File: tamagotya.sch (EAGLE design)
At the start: 34 parts, among them U100 ESP32-D2WD, U200 UT-0206-P05FOLDED, U300 4MB Flash, Y100 40Mhz 3.2X2.5

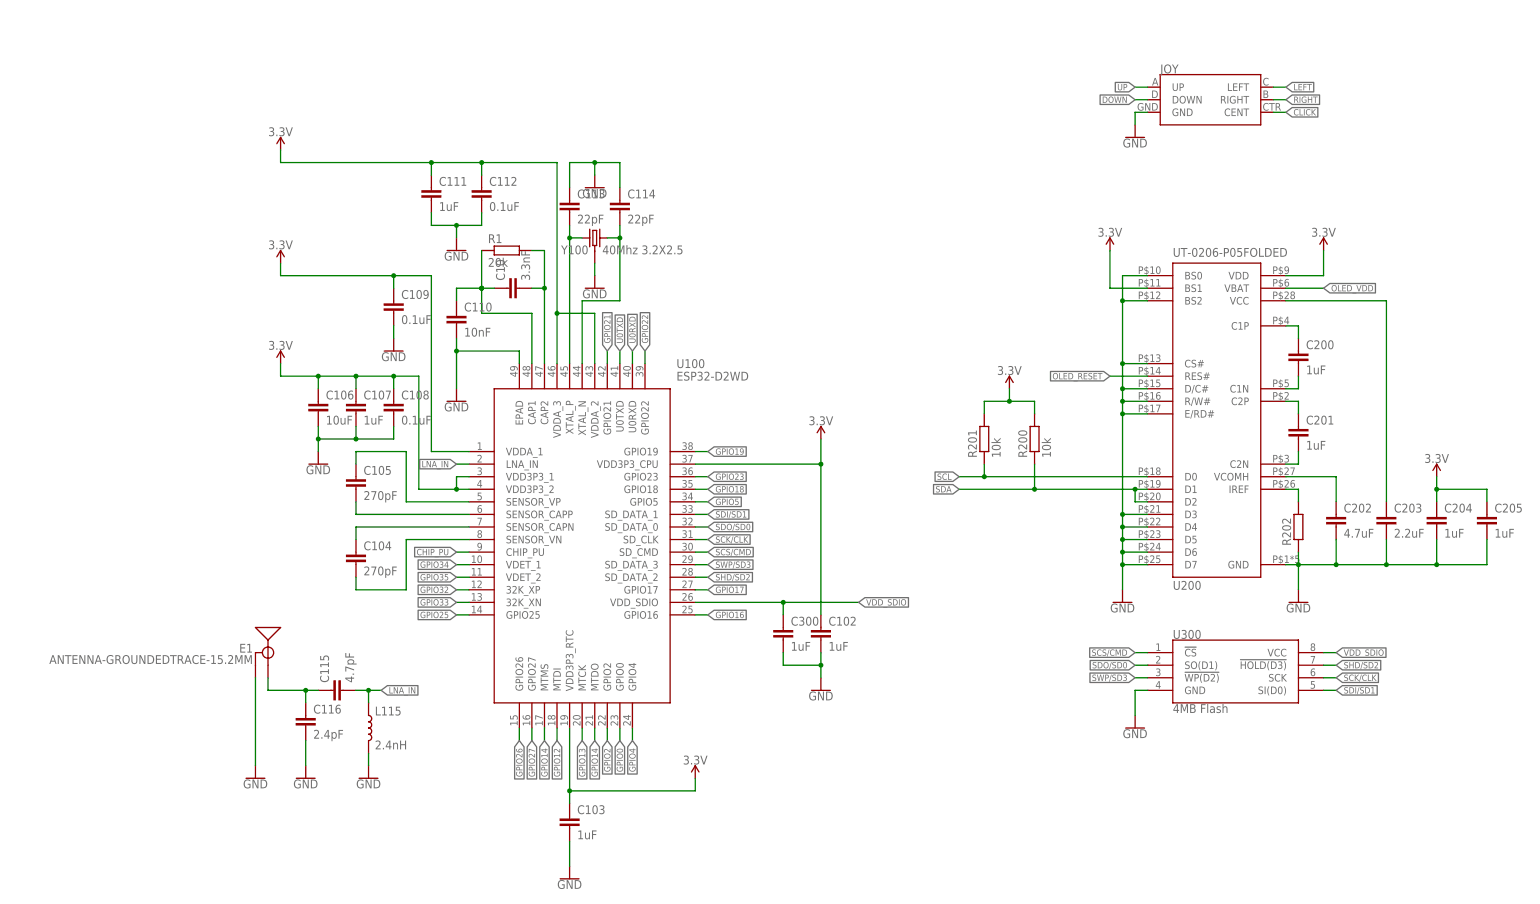
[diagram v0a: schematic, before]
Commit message: Laid out, need to add charge/boost circuit and its basically done. Could do with a UART too.
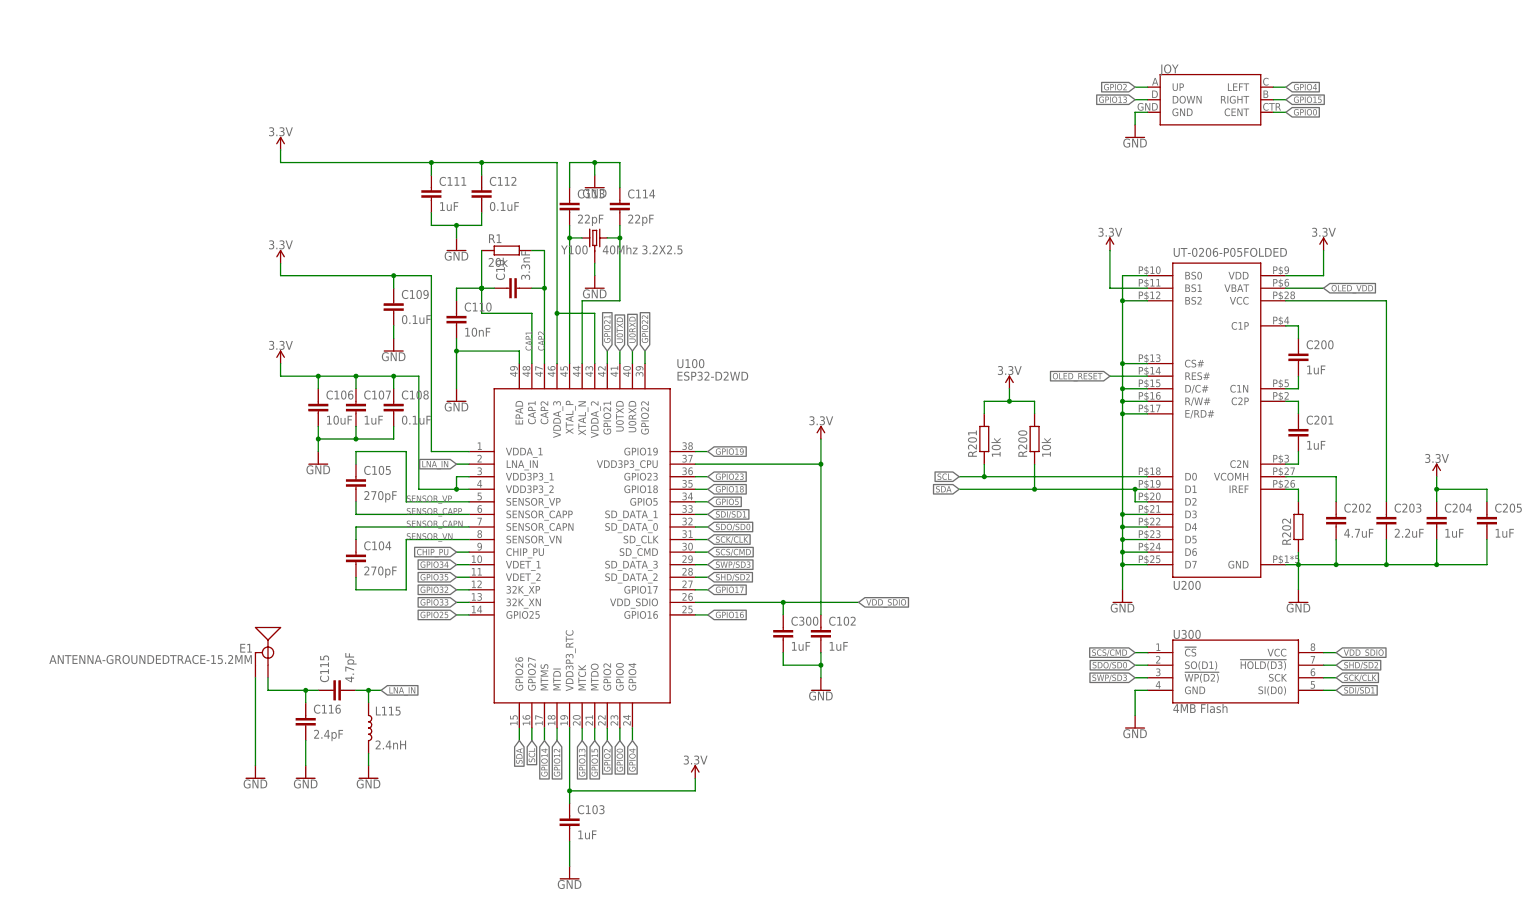
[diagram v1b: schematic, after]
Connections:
- net N$1 renamed SENSOR_VN
- net N$2 renamed SENSOR_CAPN
- net N$3 renamed SENSOR_VP
- net N$4 renamed SENSOR_CAPP
- net N$8 renamed CAP1
- net N$9 renamed CAP2
- removed net CLICK: JOY.CENT
- removed net DOWN: JOY.DOWN
- removed net GPIO26: U100.GPIO26
- removed net GPIO27: U100.GPIO27
- removed net LEFT: JOY.LEFT
- removed net RIGHT: JOY.RIGHT
- removed net UP: JOY.UP
- new net GPIO15: JOY.RIGHT, U100.MTDO
- net GPIO0: now also JOY.CENT
- net GPIO13: now also JOY.DOWN
- net GPIO14: no longer U100.MTDO
- net GPIO2: now also JOY.UP
- net GPIO4: now also JOY.LEFT
- net SCL: now also U100.GPIO27
- net SDA: now also U100.GPIO26
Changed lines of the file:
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@@
 <?xml version="1.0" encoding="utf-8"?>
 <!DOCTYPE eagle SYSTEM "eagle.dtd">
-<eagle version="9.2.2">
+<eagle version="9.3.0">
 <drawing>
 <settings>
-<setting alwaysvectorfont="yes"/>
+<setting alwaysvectorfont="no"/>
 <setting verticaltext="up"/>
 </settings>
@@
 </segment>
 </net>
-<net name="GPIO26" class="0">
-<segment>
-<pinref part="U100" gate="G$1" pin="GPIO26"/>
-<wire x1="58.42" y1="33.02" x2="58.42" y2="30.48" width="0.1524" layer="91"/>
-<label x="58.42" y="30.48" size="1.27" layer="95" rot="R270" xref="yes"/>
-</segment>
-</net>
-<net name="GPIO27" class="0">
-<segment>
-<pinref part="U100" gate="G$1" pin="GPIO27"/>
-<wire x1="60.96" y1="33.02" x2="60.96" y2="30.48" width="0.1524" layer="91"/>
-<label x="60.96" y="30.48" size="1.27" layer="95" rot="R270" xref="yes"/>
-</segment>
-</net>
 <net name="GPIO14" class="0">
 <segment>
@@
 <label x="63.5" y="30.48" size="1.27" layer="95" rot="R270" xref="yes"/>
 </segment>
-<segment>
-<pinref part="U100" gate="G$1" pin="MTDO"/>
-<wire x1="73.66" y1="33.02" x2="73.66" y2="30.48" width="0.1524" layer="91"/>
-<label x="73.66" y="30.48" size="1.27" layer="95" rot="R270" xref="yes"/>
-</segment>
 </net>
 <net name="GPIO12" class="0">
@@
 <label x="71.12" y="30.48" size="1.27" layer="95" rot="R270" xref="yes"/>
 </segment>
+<segment>
+<pinref part="JOY" gate="G$1" pin="DOWN"/>
+<wire x1="185.42" y1="160.02" x2="182.88" y2="160.02" width="0.1524" layer="91"/>
+<label x="182.88" y="160.02" size="1.27" layer="95" rot="R180" xref="yes"/>
+</segment>
 </net>
 <net name="GPIO2" class="0">
@@
 <label x="76.2" y="30.48" size="1.27" layer="95" rot="R270" xref="yes"/>
 </segment>
+<segment>
+<pinref part="JOY" gate="G$1" pin="UP"/>
+<wire x1="185.42" y1="162.56" x2="182.88" y2="162.56" width="0.1524" layer="91"/>
+<label x="182.88" y="162.56" size="1.27" layer="95" rot="R180" xref="yes"/>
+</segment>
 </net>
 <net name="GPIO0" class="0">
@@
 <label x="78.74" y="30.48" size="1.27" layer="95" rot="R270" xref="yes"/>
 </segment>
+<segment>
+<pinref part="JOY" gate="G$1" pin="CENT"/>
+<wire x1="210.82" y1="157.48" x2="213.36" y2="157.48" width="0.1524" layer="91"/>
+<label x="213.36" y="157.48" size="1.27" layer="95" xref="yes"/>
+</segment>
 </net>
 <net name="GPIO4" class="0">
@@
 <label x="81.28" y="30.48" size="1.27" layer="95" rot="R270" xref="yes"/>
 </segment>
+<segment>
+<pinref part="JOY" gate="G$1" pin="LEFT"/>
+<wire x1="210.82" y1="162.56" x2="213.36" y2="162.56" width="0.1524" layer="91"/>
+<label x="213.36" y="162.56" size="1.27" layer="95" xref="yes"/>
+</segment>
 </net>
 <net name="GPIO25" class="0">
@@
 </segment>
 </net>
-<net name="N$1" class="0">
+<net name="SENSOR_VN" class="0">
 <segment>
 <pinref part="U100" gate="G$1" pin="SENSOR_VN"/>
@@
 <pinref part="C104" gate="G$1" pin="2"/>
 <wire x1="25.4" y1="60.96" x2="25.4" y2="63.5" width="0.1524" layer="91"/>
-</segment>
-</net>
-<net name="N$2" class="0">
+<label x="35.56" y="71.12" size="1.27" layer="95"/>
+</segment>
+</net>
+<net name="SENSOR_CAPN" class="0">
 <segment>
 <pinref part="U100" gate="G$1" pin="SENSOR_CAPN"/>
@@
 <pinref part="C104" gate="G$1" pin="1"/>
 <wire x1="25.4" y1="71.12" x2="25.4" y2="73.66" width="0.1524" layer="91"/>
-</segment>
-</net>
-<net name="N$4" class="0">
+<label x="35.56" y="73.66" size="1.27" layer="95"/>
+</segment>
+</net>
+<net name="SENSOR_CAPP" class="0">
 <segment>
 <pinref part="U100" gate="G$1" pin="SENSOR_CAPP"/>
@@
 <pinref part="C105" gate="G$1" pin="2"/>
 <wire x1="25.4" y1="76.2" x2="25.4" y2="78.74" width="0.1524" layer="91"/>
-</segment>
-</net>
-<net name="N$3" class="0">
+<label x="35.56" y="76.2" size="1.27" layer="95"/>
+</segment>
+</net>
+<net name="SENSOR_VP" class="0">
 <segment>
 <pinref part="C105" gate="G$1" pin="1"/>
@@
 <pinref part="U100" gate="G$1" pin="SENSOR_VP"/>
 <wire x1="35.56" y1="78.74" x2="48.26" y2="78.74" width="0.1524" layer="91"/>
-</segment>
-</net>
-<net name="N$8" class="0">
+<label x="35.56" y="78.74" size="1.27" layer="95"/>
+</segment>
+</net>
+<net name="CAP1" class="0">
 <segment>
 <pinref part="R1" gate="G$1" pin="1"/>
@@
 <wire x1="45.72" y1="121.92" x2="50.8" y2="121.92" width="0.1524" layer="91"/>
 <junction x="50.8" y="121.92"/>
-</segment>
-</net>
-<net name="N$9" class="0">
+<label x="60.96" y="109.22" size="1.27" layer="95" rot="R90"/>
+</segment>
+</net>
+<net name="CAP2" class="0">
 <segment>
 <pinref part="R1" gate="G$1" pin="2"/>
@@
 <wire x1="63.5" y1="121.92" x2="63.5" y2="106.68" width="0.1524" layer="91"/>
 <junction x="63.5" y="121.92"/>
+<label x="63.5" y="109.22" size="1.27" layer="95" rot="R90"/>
 </segment>
 </net>
@@
 <wire x1="152.4" y1="86.36" x2="152.4" y2="83.82" width="0.1524" layer="91"/>
 <junction x="152.4" y="83.82"/>
+</segment>
+<segment>
+<pinref part="U100" gate="G$1" pin="GPIO27"/>
+<wire x1="60.96" y1="33.02" x2="60.96" y2="30.48" width="0.1524" layer="91"/>
+<label x="60.96" y="30.48" size="1.27" layer="95" rot="R270" xref="yes"/>
 </segment>
 </net>
@@
 <junction x="162.56" y="81.28"/>
 </segment>
+<segment>
+<pinref part="U100" gate="G$1" pin="GPIO26"/>
+<wire x1="58.42" y1="33.02" x2="58.42" y2="30.48" width="0.1524" layer="91"/>
+<label x="58.42" y="30.48" size="1.27" layer="95" rot="R270" xref="yes"/>
+</segment>
 </net>
 <net name="N$10" class="0">
@@
 </segment>
 </net>
-<net name="DOWN" class="0">
-<segment>
-<pinref part="JOY" gate="G$1" pin="DOWN"/>
-<wire x1="185.42" y1="160.02" x2="182.88" y2="160.02" width="0.1524" layer="91"/>
-<label x="182.88" y="160.02" size="1.27" layer="95" rot="R180" xref="yes"/>
-</segment>
-</net>
-<net name="UP" class="0">
-<segment>
-<pinref part="JOY" gate="G$1" pin="UP"/>
-<wire x1="185.42" y1="162.56" x2="182.88" y2="162.56" width="0.1524" layer="91"/>
-<label x="182.88" y="162.56" size="1.27" layer="95" rot="R180" xref="yes"/>
-</segment>
-</net>
-<net name="LEFT" class="0">
-<segment>
-<pinref part="JOY" gate="G$1" pin="LEFT"/>
-<wire x1="210.82" y1="162.56" x2="213.36" y2="162.56" width="0.1524" layer="91"/>
-<label x="213.36" y="162.56" size="1.27" layer="95" xref="yes"/>
-</segment>
-</net>
-<net name="RIGHT" class="0">
+<net name="GPIO15" class="0">
+<segment>
+<pinref part="U100" gate="G$1" pin="MTDO"/>
+<wire x1="73.66" y1="33.02" x2="73.66" y2="30.48" width="0.1524" layer="91"/>
+<label x="73.66" y="30.48" size="1.27" layer="95" rot="R270" xref="yes"/>
+</segment>
 <segment>
 <pinref part="JOY" gate="G$1" pin="RIGHT"/>
@@
 </segment>
 </net>
-<net name="CLICK" class="0">
-<segment>
-<pinref part="JOY" gate="G$1" pin="CENT"/>
-<wire x1="210.82" y1="157.48" x2="213.36" y2="157.48" width="0.1524" layer="91"/>
-<label x="213.36" y="157.48" size="1.27" layer="95" xref="yes"/>
-</segment>
-</net>

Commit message: Almost there. Mostly laid out. Just got CP2102 power to resolve.
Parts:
- added C1, C2: 22uH, rcl:C-EUC0603
- added C1503: 0.1uF, rcl:C-EUC0603
- added C3: 47uF, rcl:C-EUC0805
- added D2002: DIODE-SCHOTTKY-PMEG4005EJ, SparkFun-DiscreteSemi:DIODE-SCHOTTKY-PMEG4005EJ
- added F1: 6V/0.5A, SparkFun-Fuses:PPTC_HALF-AMP
- added L2000: 10uH, geusebio:INDUCTOR3.0X3.0
- added L2100: 4.7uH, geusebio:INDUCTOR3.0X3.0
- added NEG, POS: (no value), wirepad:SMD5
- added R1001: 1.2k, rcl:R-EU_R0603
- added R1006, R1007, R1501, R2005, R2103: 1k, rcl:R-EU_R0603
- added R1008, R1009: 2k, rcl:R-EU_R0603
- added R2: 10k, rcl:R-EU_R0603
- added R2004: 7.5k, rcl:R-EU_R0603
- added R2102: 4.5k, rcl:R-EU_R0603
- added U$2: USB-C, geusebio:USB-C
- added U$3: CP2102N-QFN24, geusebio:CP2102N-QFN24
- added U1000: TP4056, geusebio:TP4056
- added U1500: FS312F-G, geusebio:FS312F-G
- added U1550: FS8205, geusebio:FS8205
- added U2000: MT3608, geusebio:MT3608
- added U2100: M3406, geusebio:M3406
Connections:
- net N$5 renamed XTAL_P
- net N$6 renamed XTAN_N
- removed net CHIP_PU: U100.CHIP_PU
- removed net U0RXD: U100.U0RXD
- removed net U0TXD: U100.U0TXD
- new net 5V: C2.1, D2002.C, R2004.2, U2100.RUN, U2100.VIN
- new net BUCK: D2002.A, L2000.2, U2000.SW
- new net CHRG: R1006.2, U1000.CHRG
- new net CHRG_3V3: R1006.1, R1008.2
- new net D+: U$2.D+, U$3.D+
- new net D-: U$2.D-, U$3.D-
- new net FS_CS: R1501.2, U1500.CS
- new net GND_BATT: C1503.2, NEG.P, R1501.1, U1500.GND, U1550.S2
- new net N$17: U$3.VIO
- new net N$18: U$3.VDD
- new net N$20: U$3.RI/CLK
- new net N$21: U$3.DCD
- new net N$23: U$3.DSR
- new net N$26: U$3.CTS
- new net N$27: U$3.SUSPEND
- new net N$28: U$3.SUSPENDB
- new net N$29: U$3.GPIO.0
- new net N$3: R2004.1, R2005.2, U2000.FB
- new net N$30: U$3.GPIO.1
- new net N$31: U$3.GPIO.2
- new net N$32: U$3.GPIO.3
- new net N$33: U$3.RSTB
- new net N$35: U$3.VBUS
- new net N$36: U$3.VREGIN
- new net N$4: R1001.2, U1000.PROG
- new net N$8: L2100.1, U2100.SW
- new net N$9: R2102.1, R2103.2, U2100.FB
- new net OC: U1500.OC, U1550.G1
- new net OD: U1500.OD, U1550.G2
- new net RESET: R2.1, U$3.RTS, U100.CHIP_PU
- new net STDBY: R1007.2, U1000.STDBY
- new net STDBY_3V3: R1007.1, R1009.2
- new net U100RXD: U$3.TXD, U100.U0RXD
- new net U100TXD: U$3.RXD, U100.U0TXD
- new net V_BATT: C1.1, C1503.1, L2000.1, POS.P, U1000.BAT, U1500.VCC, U2000.EN, U2000.IN
- new net V_USB: F1.1, U1000.CE, U1000.VCC
- new net V_USB_UNFUSED: F1.2, U$2.VBUS
- net 3.3V: now also C3.1, L2100.2, R2.2, R2102.2
- net GND: now also C1.2, C2.2, C3.2, R1001.1, R1008.1, R1009.1, R2005.1, R2103.1, U$2.GND, U$3.GND, U1000.GND, U1000.TEMP, U1550.S1, U2000.GND, U2100.GND
- net GPIO0: now also U$3.DTR
